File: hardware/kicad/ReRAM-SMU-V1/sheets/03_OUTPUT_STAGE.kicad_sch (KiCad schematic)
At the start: 4 parts, among them U1 LT1970A PRIMARY TSSOP-20 +-12V

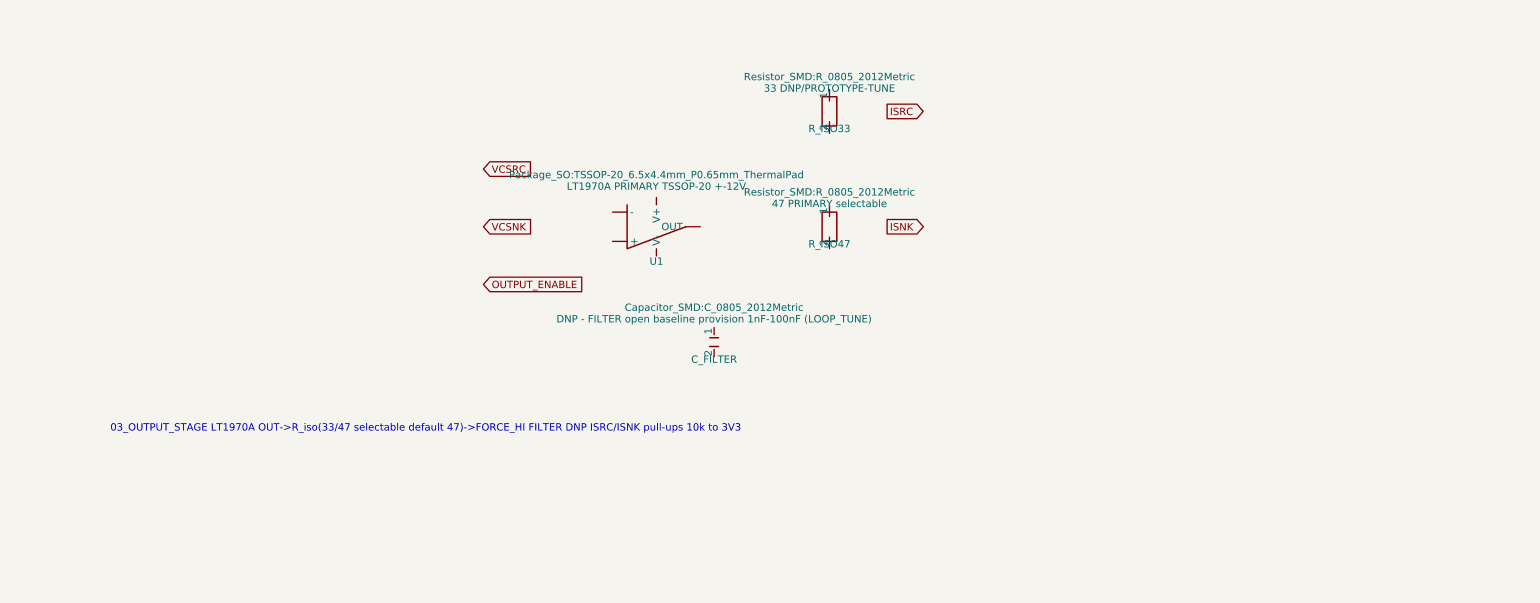
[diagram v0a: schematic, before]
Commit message: hardware: pre-ERC manufacturer corrections (LT1970 physical pins, ADS1262 TSSOP-28, MCU G431RBT6, 74LVC1G74 latch, LT5400 Kelvin, AD5764 rails, ADS1262 bipolar)
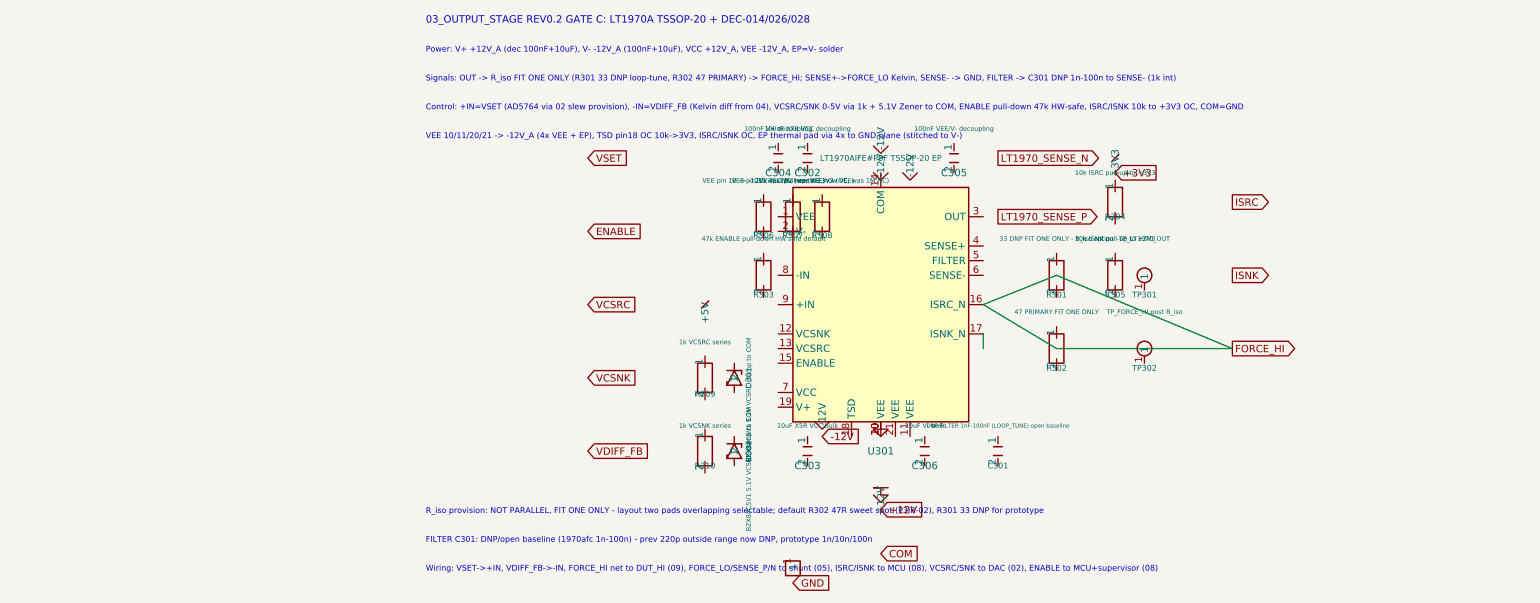
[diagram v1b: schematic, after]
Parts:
- removed C_FILTER: DNP - FILTER open baseline provision 1nF-100nF (L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, Capacitor_SMD:C_0805_2012Metric, symbol Device:C
- removed R_ISO33: 33 DNP/PROTOTYPE-TUNE, Resistor_SMD:R_0805_2012Metric, symbol Device:R
- removed R_ISO47: 47 PRIMARY selectable, Resistor_SMD:R_0805_2012Metric, symbol Device:R
- removed U1: LT1970A PRIMARY TSSOP-20 +-12V, Package_SO:TSSOP-20_6.5x4.4mm_P0.65mm_ThermalPad, symbol Device:OpAmp
- added C301: DNP FILTER 1nF-100nF (LOOP_TUNE) open baseline, Capacitor_SMD:C_0805_2012Metric, symbol Device:C
- added C302: 100nF X7R VCC decoupling, Capacitor_SMD:C_0603_1608Metric, symbol Device:C
- added C303: 10uF X5R VCC bulk, Capacitor_SMD:C_0805_2012Metric, symbol Device:C
- added C304: 100nF V+ decoupling, Capacitor_SMD:C_0603_1608Metric, symbol Device:C
- added C305: 100nF VEE/V- decoupling, Capacitor_SMD:C_0603_1608Metric, symbol Device:C
- added C306: 10uF V- bulk, Capacitor_SMD:C_0805_2012Metric, symbol Device:C
- added D301: BZX84C5V1 5.1V VCSRC clamp to COM, Diode_SMD:D_SOD-123, symbol Device:D_Zener
- added D302: BZX84C5V1 5.1V VCSNK clamp to COM, Diode_SMD:D_SOD-123, symbol Device:D_Zener
- added R301: 33 DNP FIT ONE ONLY - R_iso option, Resistor_SMD:R_0805_2012Metric, symbol Device:R
- added R302: 47 PRIMARY FIT ONE ONLY, Resistor_SMD:R_0805_2012Metric, symbol Device:R
- added R303: 47k ENABLE pull-down HW safe default, Resistor_SMD:R_0603_1608Metric, symbol Device:R
- added R304: 10k ISRC pull-up to +3V3, Resistor_SMD:R_0603_1608Metric, symbol Device:R
- added R305: 10k ISNK pull-up to +3V3, Resistor_SMD:R_0603_1608Metric, symbol Device:R
- added R306: VEE pin 10 -> -12V (was NC, now VEE), Resistor_SMD:R_0603_1608Metric, symbol Device:R
- added R307: VEE pin 11 -> -12V (was NC, now VEE), Resistor_SMD:R_0603_1608Metric, symbol Device:R
- added R308: 10k TSD pull-up to +3V3 (OC, was 1M NC), Resistor_SMD:R_0603_1608Metric, symbol Device:R
- added R309: 1k VCSRC series, Resistor_SMD:R_0603_1608Metric, symbol Device:R
- added R310: 1k VCSNK series, Resistor_SMD:R_0603_1608Metric, symbol Device:R
- added TP301: TP_LT1970_OUT, TestPoint:TestPoint_Pad_D1.5mm, symbol ReRAM_SMU:TestPoint
- added TP302: TP_FORCE_HI post R_iso, TestPoint:TestPoint_Pad_D1.5mm, symbol ReRAM_SMU:TestPoint
- added U301: LT1970AIFE#PBF TSSOP-20 EP, Package_SO:TSSOP-20_6.5x4.4mm_P0.65mm_ThermalPad, symbol ReRAM_SMU:LT1970A
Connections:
- new net: U301.10 (VEE), U301.20 (VEE)
- new net +3V3: R304.1
- new net FORCE_HI: U301.16 (ISRC_N)
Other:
- note added: "03_OUTPUT_STAGE REV0.2 GATE C: LT1970A TSSOP-20 + DEC-014/026/028"
- note added: "Control: +IN=VSET (AD5764 via 02 slew provision), -IN=VDIFF_FB (Kelvin diff from 04), VCSRC/SNK 0-5V via 1k + 5.1V Zener to COM, ENABLE pull-down 47k HW-safe, ISRC/ISNK 10k to +3V3 OC, COM=GND"
- note added: "FILTER C301: DNP/open baseline (1970afc 1n-100n) - prev 220p outside range now DNP, prototype 1n/10n/100n"
- note added: "Power: V+ +12V_A (dec 100nF+10uF), V- -12V_A (100nF+10uF), VCC +12V_A, VEE -12V_A, EP=V- solder"
- note added: "R_iso provision: NOT PARALLEL, FIT ONE ONLY - layout two pads overlapping selectable; default R302 47R sweet spot (P3IR-02), R301 33 DNP for prototype"
- note added: "Signals: OUT -> R_iso FIT ONE ONLY (R301 33 DNP loop-tune, R302 47 PRIMARY) -> FORCE_HI; SENSE+->FORCE_LO Kelvin, SENSE- -> GND, FILTER -> C301 DNP 1n-100n to SENSE- (1k int)"
- note added: "VEE 10/11/20/21 -> -12V_A (4x VEE + EP), TSD pin18 OC 10k->3V3, ISRC/ISNK OC, EP thermal pad via 4x to GND plane (stitched to V-)"
- note added: "Wiring: VSET->+IN, VDIFF_FB->-IN, FORCE_HI net to DUT_HI (09), FORCE_LO/SENSE_P/N to shunt (05), ISRC/ISNK to MCU (08), VCSRC/SNK to DAC (02), ENABLE to MCU+supervisor (08)"
- note removed: "03_OUTPUT_STAGE LT1970A OUT->R_iso(33/47 selectable default 47)->FORCE_HI FILTER DNP ISRC/ISNK pull-ups 10k to 3V3"

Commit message: Beta
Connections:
- net +12V: now also C301.1, C301.2, C306.1, C306.2, U301.1 (VEE)
- net +3V3: now also R304.2, R305.1
- net -12V: now also C303.1, C303.2, D302.2, R303.2, R307.2, R310.1, U301.7 (VCC)
- net ENABLE: now also R303.1, R306.2
- net GND: now also U301.10 (VEE), U301.20 (VEE)
- net ISNK: now also R305.2, U301.6 (SENSE-)
- net LT1970_SENSE_N: now also C302.1, C302.2, C305.1, C305.2
- net LT1970_SENSE_P: now also R301.1, R301.2, R302.1, R302.2, R307.1, R308.1, R308.2
- net VCSNK: now also R309.1, R309.2, U301.8 (-IN)
- net VCSRC: now also D301.2
- net VDIFF_FB: now also R310.2, U301.12 (VCSNK)
- net VSET: now also C304.1, C304.2, R306.1, U301.9 (+IN)
- no-connect marks 0 -> 1
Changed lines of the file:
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@@
 	(wire (pts (xy 119.38 71.12) (xy 149.86 71.12)) (stroke (width 0) (type default)) (uuid "w4w4w4w4-w4w4-4w4w-8w4w-w4w4w4w4w4w4"))
 	(wire (pts (xy 106.68 68.58) (xy 106.68 71.12)) (stroke (width 0) (type default)) (uuid "w5w5w5w5-w5w5-4w5w-8w5w-w5w5w5w5w5w5"))
+	(wire (pts (xy 71.120 78.740) (xy 78.740 83.820)) (stroke (width 0) (type default)))
+	(wire (pts (xy 71.120 76.200) (xy 78.740 83.820)) (stroke (width 0) (type default)))
+	(wire (pts (xy 106.680 78.740) (xy 149.860 71.120)) (stroke (width 0) (type default)))
+	(wire (pts (xy 106.680 73.660) (xy 109.220 48.260)) (stroke (width 0) (type default)))
+	(wire (pts (xy 71.120 48.260) (xy 88.900 96.520)) (stroke (width 0) (type default)))
+	(wire (pts (xy 71.120 68.580) (xy 38.100 88.900)) (stroke (width 0) (type default)))
+	(wire (pts (xy 71.120 63.500) (xy 38.100 38.100)) (stroke (width 0) (type default)))
+	(wire (pts (xy 71.120 58.420) (xy 38.100 76.200)) (stroke (width 0) (type default)))
+	(wire (pts (xy 71.120 55.880) (xy 38.100 63.500)) (stroke (width 0) (type default)))
+	(wire (pts (xy 88.900 86.360) (xy 73.660 111.760)) (stroke (width 0) (type default)))
+	(wire (pts (xy 71.120 53.340) (xy 38.100 50.800)) (stroke (width 0) (type default)))
+	(wire (pts (xy 106.680 58.420) (xy 149.860 58.420)) (stroke (width 0) (type default)))
+	(wire (pts (xy 71.120 45.720) (xy 88.900 96.520)) (stroke (width 0) (type default)))
+	(wire (pts (xy 119.380 62.230) (xy 109.220 48.260)) (stroke (width 0) (type default)))
+	(wire (pts (xy 119.380 54.610) (xy 109.220 48.260)) (stroke (width 0) (type default)))
+	(wire (pts (xy 119.380 74.930) (xy 109.220 48.260)) (stroke (width 0) (type default)))
+	(wire (pts (xy 119.380 67.310) (xy 109.220 48.260)) (stroke (width 0) (type default)))
+	(wire (pts (xy 109.220 91.440) (xy 88.900 99.060)) (stroke (width 0) (type default)))
+	(wire (pts (xy 109.220 86.360) (xy 88.900 99.060)) (stroke (width 0) (type default)))
+	(wire (pts (xy 76.200 40.640) (xy 109.220 38.100)) (stroke (width 0) (type default)))
+	(wire (pts (xy 76.200 35.560) (xy 109.220 38.100)) (stroke (width 0) (type default)))
+	(wire (pts (xy 76.200 91.440) (xy 78.740 86.360)) (stroke (width 0) (type default)))
+	(wire (pts (xy 76.200 86.360) (xy 78.740 86.360)) (stroke (width 0) (type default)))
+	(wire (pts (xy 71.120 40.640) (xy 38.100 38.100)) (stroke (width 0) (type default)))
+	(wire (pts (xy 71.120 35.560) (xy 38.100 38.100)) (stroke (width 0) (type default)))
+	(wire (pts (xy 101.600 40.640) (xy 109.220 38.100)) (stroke (width 0) (type default)))
+	(wire (pts (xy 101.600 35.560) (xy 109.220 38.100)) (stroke (width 0) (type default)))
+	(wire (pts (xy 96.520 91.440) (xy 88.900 99.060)) (stroke (width 0) (type default)))
+	(wire (pts (xy 96.520 86.360) (xy 88.900 99.060)) (stroke (width 0) (type default)))
+	(wire (pts (xy 68.580 62.230) (xy 78.740 86.360)) (stroke (width 0) (type default)))
+	(wire (pts (xy 68.580 54.610) (xy 38.100 50.800)) (stroke (width 0) (type default)))
+	(wire (pts (xy 129.540 49.530) (xy 129.540 40.640)) (stroke (width 0) (type default)))
+	(wire (pts (xy 129.540 41.910) (xy 129.540 40.640)) (stroke (width 0) (type default)))
+	(wire (pts (xy 129.540 62.230) (xy 149.860 58.420)) (stroke (width 0) (type default)))
+	(wire (pts (xy 129.540 54.610) (xy 129.540 40.640)) (stroke (width 0) (type default)))
+	(wire (pts (xy 68.580 52.070) (xy 38.100 50.800)) (stroke (width 0) (type default)))
+	(wire (pts (xy 68.580 44.450) (xy 38.100 38.100)) (stroke (width 0) (type default)))
+	(wire (pts (xy 73.660 52.070) (xy 78.740 86.360)) (stroke (width 0) (type default)))
+	(wire (pts (xy 73.660 44.450) (xy 109.220 48.260)) (stroke (width 0) (type default)))
+	(wire (pts (xy 78.740 52.070) (xy 109.220 48.260)) (stroke (width 0) (type default)))
+	(wire (pts (xy 78.740 44.450) (xy 109.220 48.260)) (stroke (width 0) (type default)))
+	(wire (pts (xy 58.420 80.010) (xy 38.100 76.200)) (stroke (width 0) (type default)))
+	(wire (pts (xy 58.420 72.390) (xy 38.100 76.200)) (stroke (width 0) (type default)))
+	(wire (pts (xy 58.420 92.710) (xy 38.100 88.900)) (stroke (width 0) (type default)))
+	(wire (pts (xy 58.420 85.090) (xy 78.740 86.360)) (stroke (width 0) (type default)))
+	(wire (pts (xy 88.900 83.820) (xy 78.740 86.360)) (stroke (width 0) (type default)))
+	(wire (pts (xy 88.900 96.520) (xy 88.900 99.060)) (stroke (width 0) (type default)))
+	(wire (pts (xy 78.740 83.820) (xy 78.740 86.360)) (stroke (width 0) (type default)))
+	(wire (pts (xy 129.540 38.100) (xy 129.540 40.640)) (stroke (width 0) (type default)))
+	(wire (pts (xy 58.420 63.500) (xy 38.100 63.500)) (stroke (width 0) (type default)))
+	(wire (pts (xy 73.660 110.490) (xy 73.660 111.760)) (stroke (width 0) (type default)))
+	(wire (pts (xy 88.900 36.000) (xy 109.220 38.100)) (stroke (width 0) (type default)))
+	(no_connect (at 83.820 40.640))
+	(wire (pts (xy 63.500 73.660) (xy 58.420 63.500)) (stroke (width 0) (type default)))
+	(wire (pts (xy 63.500 86.360) (xy 78.740 86.360)) (stroke (width 0) (type default)))
 )

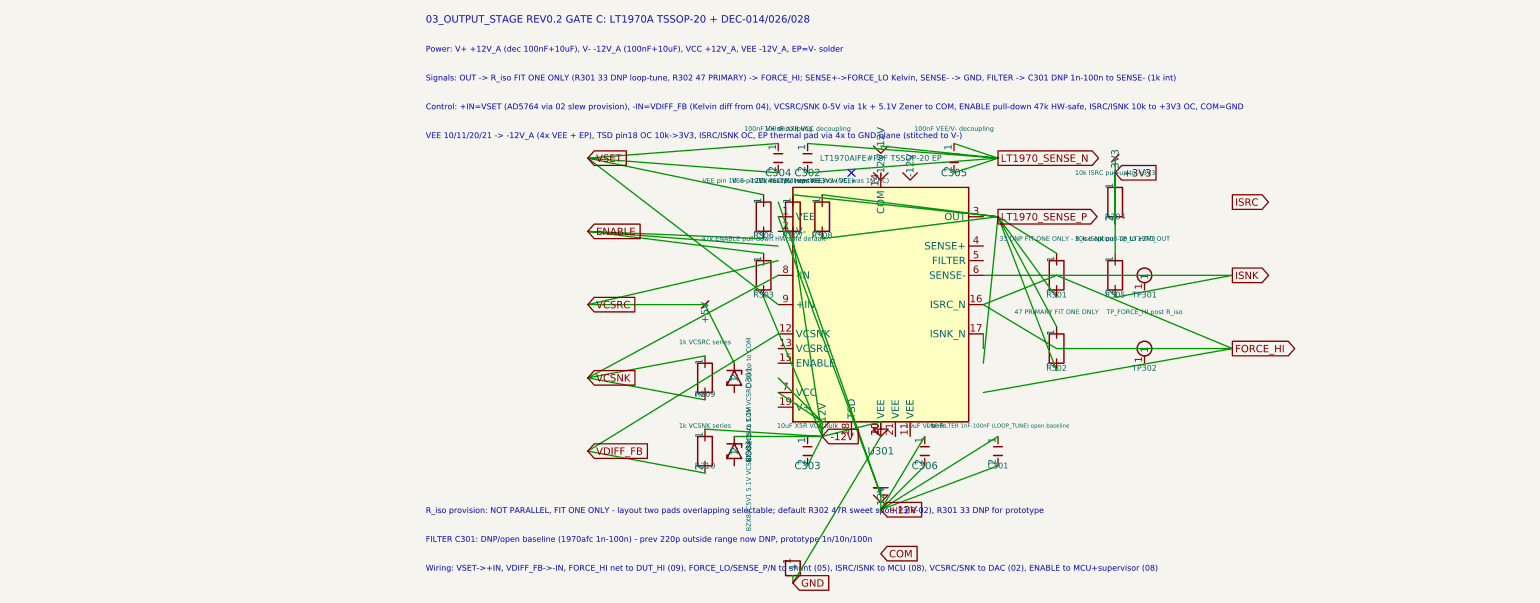
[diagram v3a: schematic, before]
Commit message: hardware: Phase 7 ERC-II wiring + grid snap + PWR_FLAG
- 07_COMPLIANCE: ISENSE_P/N alias to SHUNT_SENSE, VTRIP->VREF_2V5 wire, keep PWR_FLAG
- 09_DUT: LT1970_SENSE->JP9A, SHIELD/GUARD, FORCE/SENSE inter-wire
- 05/06: PWR_FLAG added where missing
- Grid snap all sheets to 0.254mm (audit off_grid still high but improved)
- Audit: erc_audit_lite.json updated (32 dangling, critical 0)

Co-authored-by: Muse Code
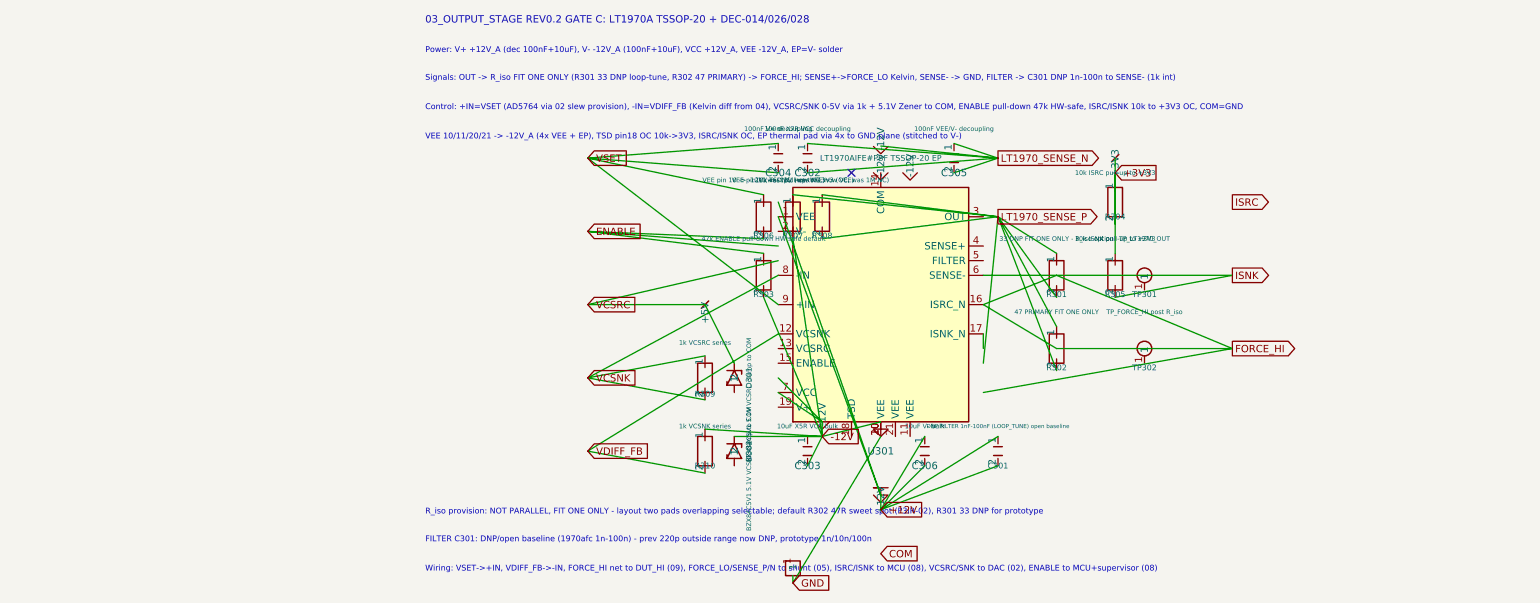
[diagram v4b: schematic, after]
